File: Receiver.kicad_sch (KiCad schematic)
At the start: 37 parts, among them SW2 TS2306A, U19 ESP32-C3, U20 AT2401C, U21 TPRT9013-33, U22 SX1280IMLTRT, Y2 40MHz, Y3 52MHz/10ppm

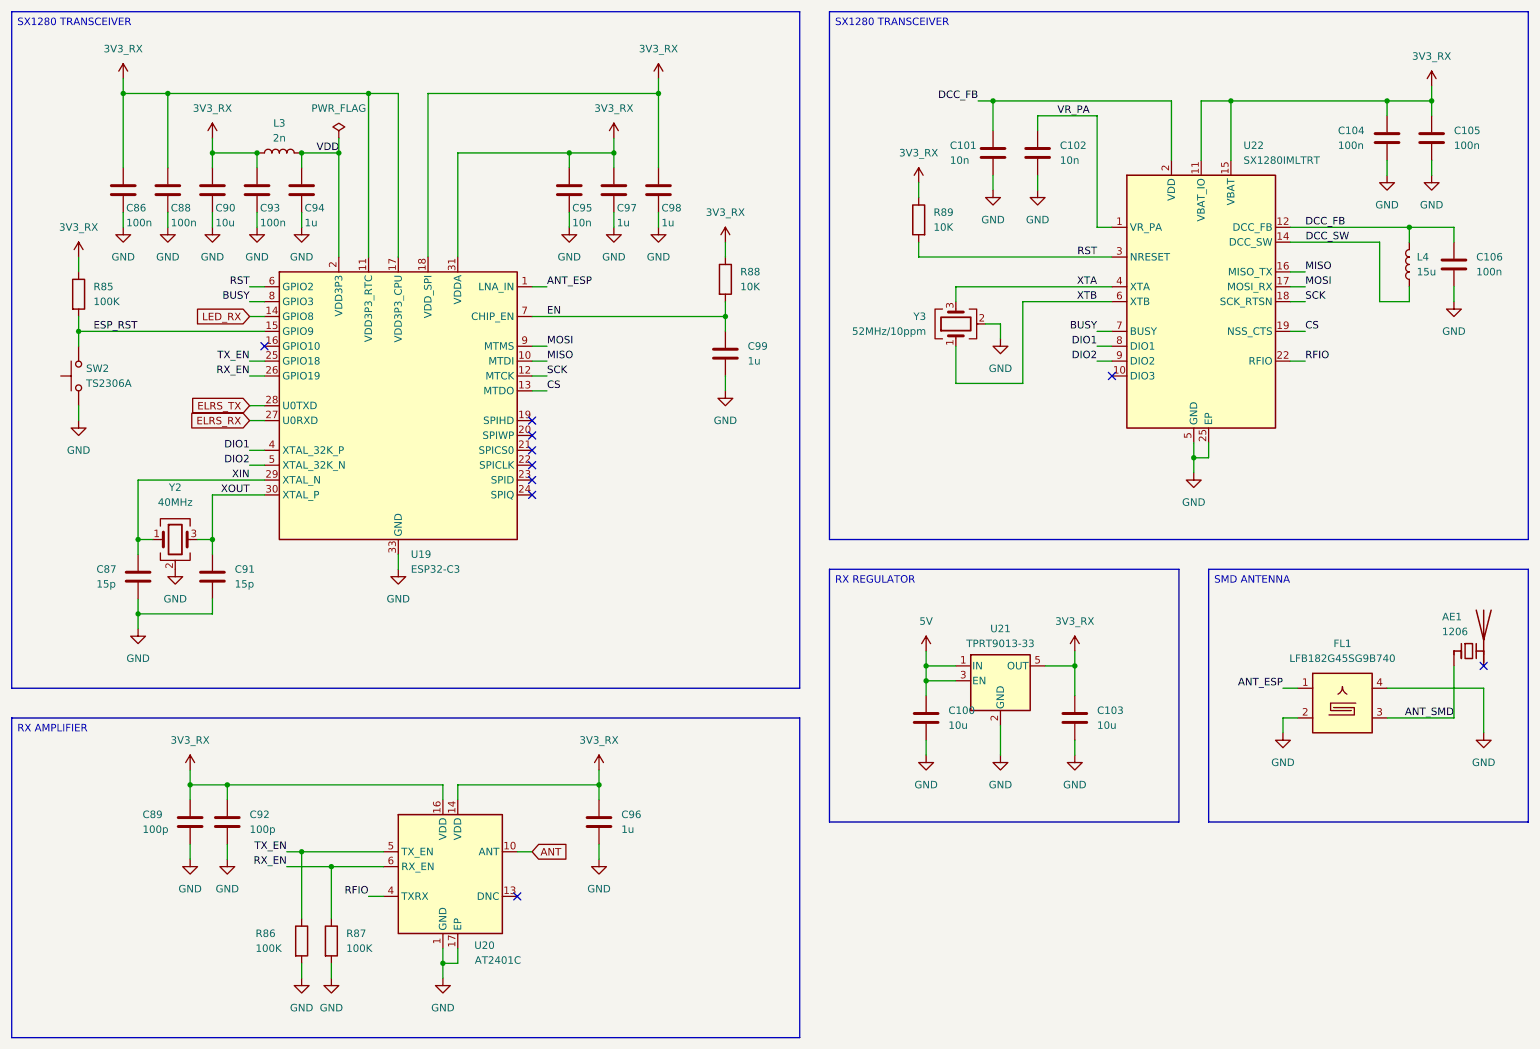
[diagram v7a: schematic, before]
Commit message: IMU filtering and layout
Added a missing capacitor for the IMU.
Updated the PCB layout.
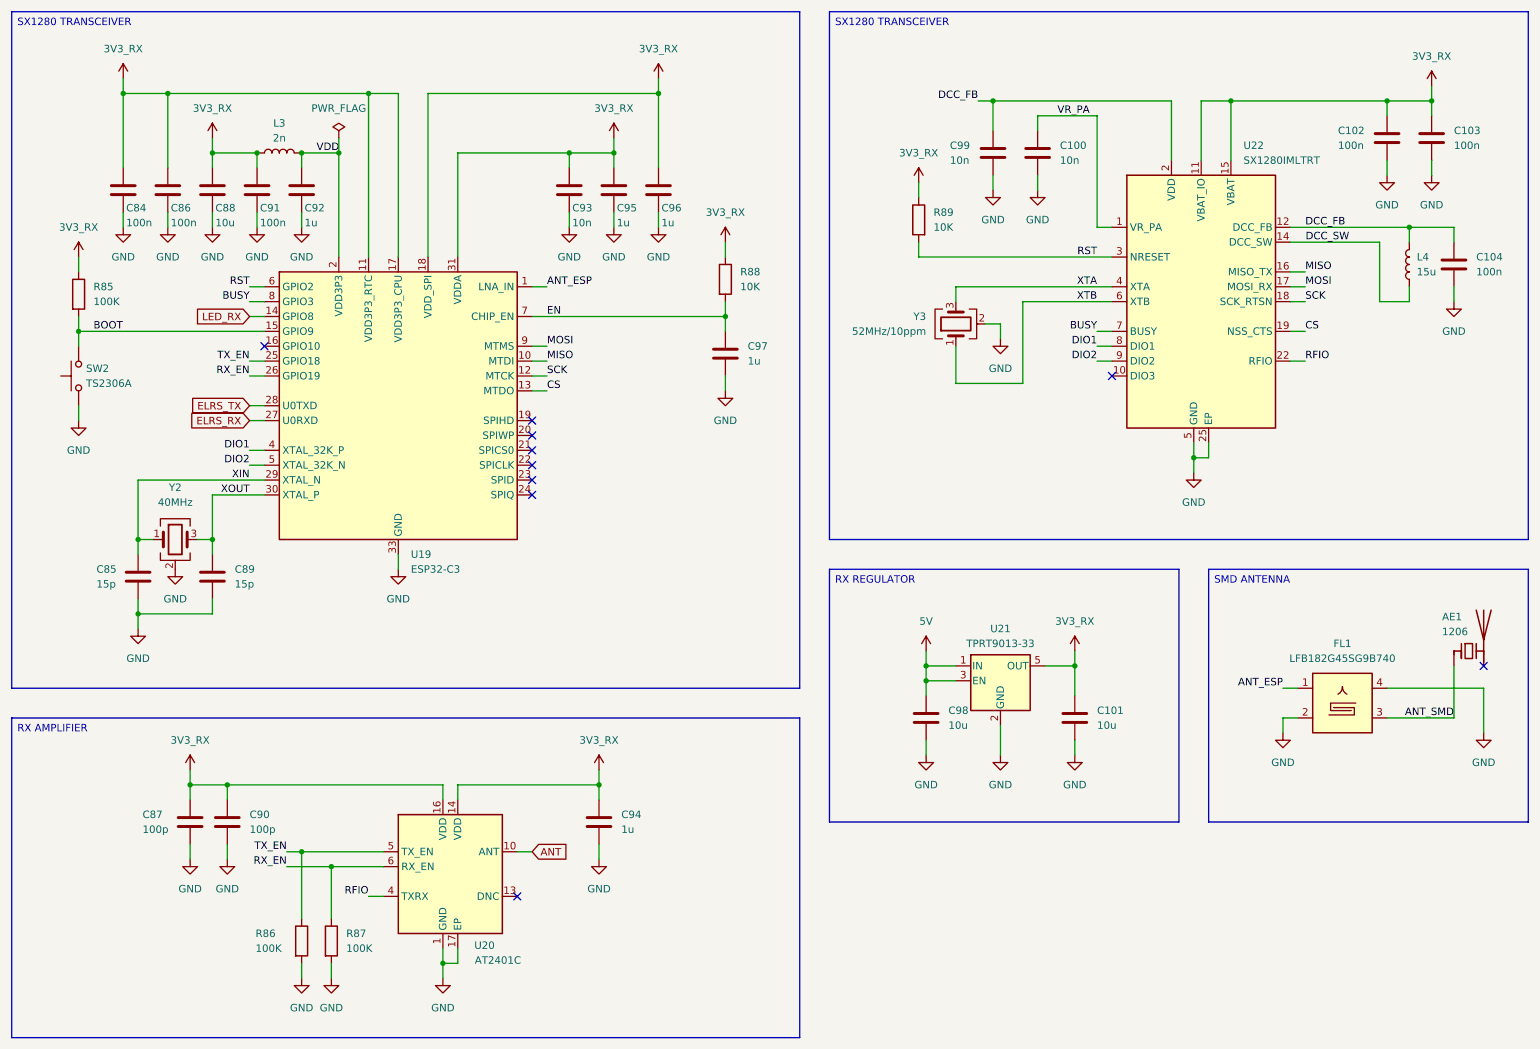
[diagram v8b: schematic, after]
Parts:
- renumbered C102 to C100, C103 to C101, C104 to C102, C105 to C103, C106 to C104, C86 to C84, C87 to C85, C88 to C86, C89 to C87, C90 to C88, C91 to C89, C92 to C90, C93 to C91, C94 to C92, C95 to C93, C96 to C94, C97 to C95, C98 to C96, C99 to C97, C100 to C98, C101 to C99
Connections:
- net ESP_RST renamed BOOT
